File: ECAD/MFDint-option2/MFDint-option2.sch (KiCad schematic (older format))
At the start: 40 parts, among them J1 Conn_02x03_Odd_Even, J2 Conn_01x04, J3 Conn_01x04, J4 Conn_02x03_Odd_Even, J5 Conn_01x04, J6 Conn_01x04, SW11 SW_Push, SW12 SW_Push, SW13 SW_Push, SW14 SW_Push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

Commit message: Removing panelisations, adding polyfuses
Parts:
- added F1, F2: Polyfuse, Fuse:Fuse_1206_3216Metric_Pad1.42x1.75mm_HandSolder, symbol Device:Polyfuse
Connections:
- wire segments 176 -> 184
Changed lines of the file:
@@
 	1    0    0    -1
 $EndComp
-$Comp
-L power:+5V #PWR0104
-U 1 1 60C40200
-P 3650 750
-F 0 "#PWR0104" H 3650 600 50  0001 C CNN
-F 1 "+5V" H 3665 923 50  0000 C CNN
-F 2 "" H 3650 750 50  0001 C CNN
-F 3 "" H 3650 750 50  0001 C CNN
-	1    3650 750
-	1    0    0    -1
-$EndComp
-Wire Wire Line
-	3650 750  3700 750
 Wire Wire Line
 	3700 850  3650 850
@@
 L power:+5V #PWR0108
 U 1 1 60D08791
-P 3650 1500
-F 0 "#PWR0108" H 3650 1350 50  0001 C CNN
-F 1 "+5V" H 3665 1673 50  0000 C CNN
-F 2 "" H 3650 1500 50  0001 C CNN
-F 3 "" H 3650 1500 50  0001 C CNN
-	1    3650 1500
-	1    0    0    -1
-$EndComp
-Wire Wire Line
-	3650 1500 3700 1500
+P 4900 600
+F 0 "#PWR0108" H 4900 450 50  0001 C CNN
+F 1 "+5V" H 4915 773 50  0000 C CNN
+F 2 "" H 4900 600 50  0001 C CNN
+F 3 "" H 4900 600 50  0001 C CNN
+	1    4900 600
+	1    0    0    -1
+$EndComp
 Wire Wire Line
 	3700 1600 3650 1600
@@
 	1    0    0    -1
 $EndComp
-Wire Wire Line
-	9350 950  9400 950
 Wire Wire Line
 	9400 1050 9350 1050
@@
 	1    0    0    -1
 $EndComp
-Wire Wire Line
-	9350 1700 9400 1700
 Wire Wire Line
 	9400 1800 9350 1800
@@
 L power:VCC #PWR0113
 U 1 1 60DE50D9
-P 9350 950
-F 0 "#PWR0113" H 9350 800 50  0001 C CNN
-F 1 "VCC" H 9365 1123 50  0000 C CNN
-F 2 "" H 9350 950 50  0001 C CNN
-F 3 "" H 9350 950 50  0001 C CNN
-	1    9350 950
-	1    0    0    -1
-$EndComp
-$Comp
-L power:VCC #PWR0114
-U 1 1 60DEBA77
-P 9350 1700
-F 0 "#PWR0114" H 9350 1550 50  0001 C CNN
-F 1 "VCC" H 9365 1873 50  0000 C CNN
-F 2 "" H 9350 1700 50  0001 C CNN
-F 3 "" H 9350 1700 50  0001 C CNN
-	1    9350 1700
+P 10600 800
+F 0 "#PWR0113" H 10600 650 50  0001 C CNN
+F 1 "VCC" H 10615 973 50  0000 C CNN
+F 2 "" H 10600 800 50  0001 C CNN
+F 3 "" H 10600 800 50  0001 C CNN
+	1    10600 800
 	1    0    0    -1
 $EndComp
@@
 Wire Wire Line
 	9750 5250 10650 5250
+$Comp
+L Device:Polyfuse F1
+U 1 1 60F99DDE
+P 4600 600
+F 0 "F1" V 4375 600 50  0000 C CNN
+F 1 "Polyfuse" V 4466 600 50  0000 C CNN
+F 2 "Fuse:Fuse_1206_3216Metric_Pad1.42x1.75mm_HandSolder" H 4650 400 50  0001 L CNN
+F 3 "~" H 4600 600 50  0001 C CNN
+	1    4600 600
+	0    1    1    0
+$EndComp
+Wire Wire Line
+	3400 750  3400 1500
+Wire Wire Line
+	3400 750  3700 750
+Wire Wire Line
+	3400 1500 3700 1500
+Wire Wire Line
+	3400 750  3400 600
+Wire Wire Line
+	3400 600  4450 600
+Connection ~ 3400 750
+Wire Wire Line
+	4750 600  4900 600
+Wire Wire Line
+	9100 950  9100 1700
+Wire Wire Line
+	9100 950  9100 800
+Wire Wire Line
+	9100 800  10150 800
+Connection ~ 9100 950
+Wire Wire Line
+	9100 950  9400 950
+Wire Wire Line
+	9100 1700 9400 1700
+$Comp
+L Device:Polyfuse F2
+U 1 1 60FC34AB
+P 10300 800
+F 0 "F2" V 10075 800 50  0000 C CNN
+F 1 "Polyfuse" V 10166 800 50  0000 C CNN
+F 2 "Fuse:Fuse_1206_3216Metric_Pad1.42x1.75mm_HandSolder" H 10350 600 50  0001 L CNN
+F 3 "~" H 10300 800 50  0001 C CNN
+	1    10300 800
+	0    1    1    0
+$EndComp
+Wire Wire Line
+	10450 800  10600 800
 $EndSCHEMATC

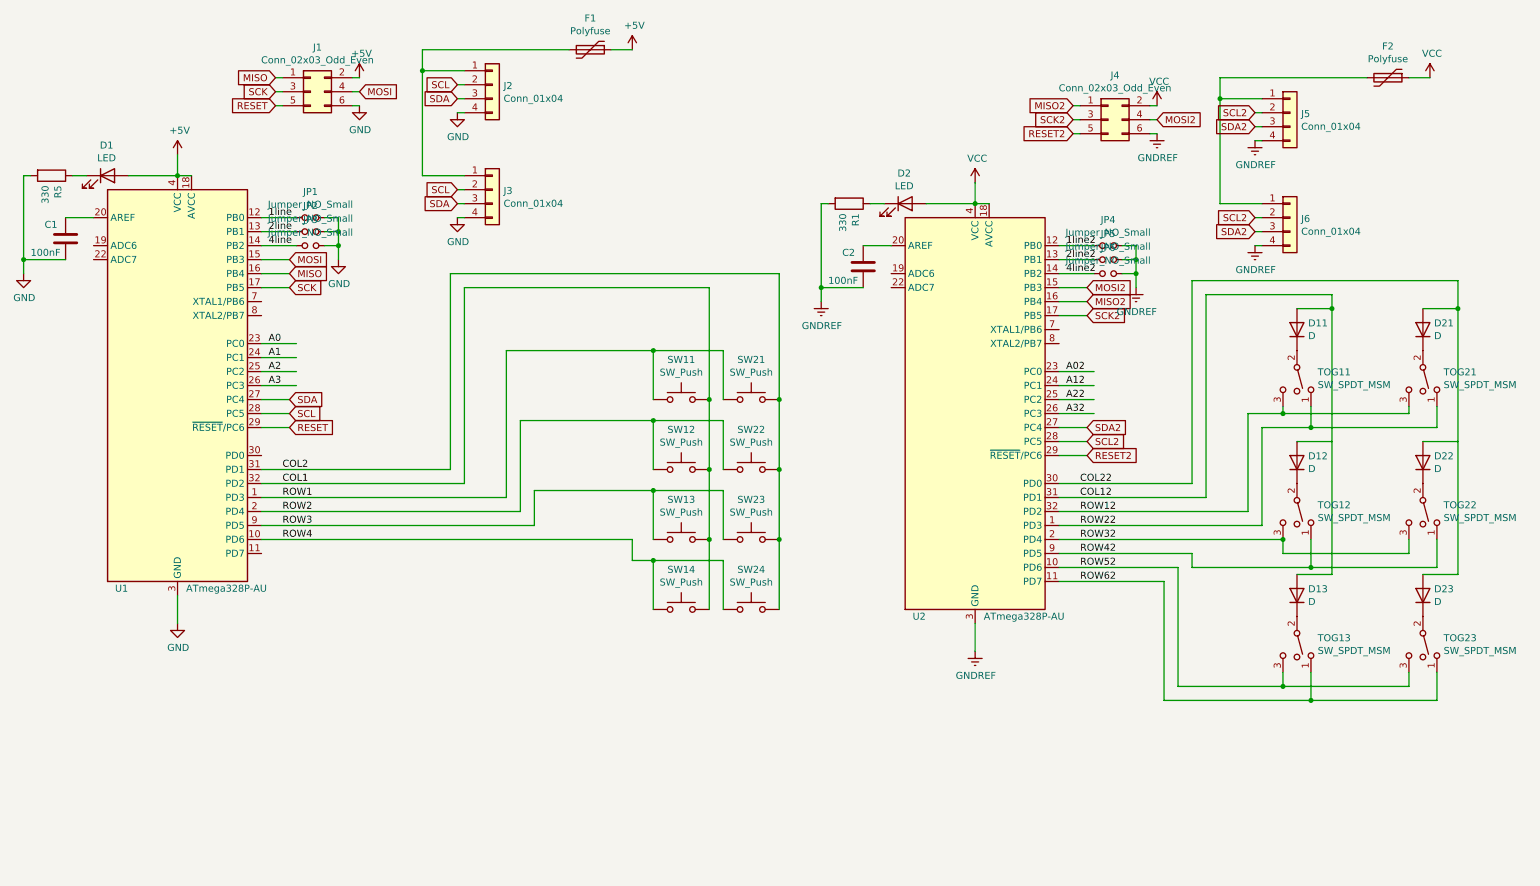
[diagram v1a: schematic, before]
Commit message: Change from 1x04 2.54mm headers to 1x05 micro JST
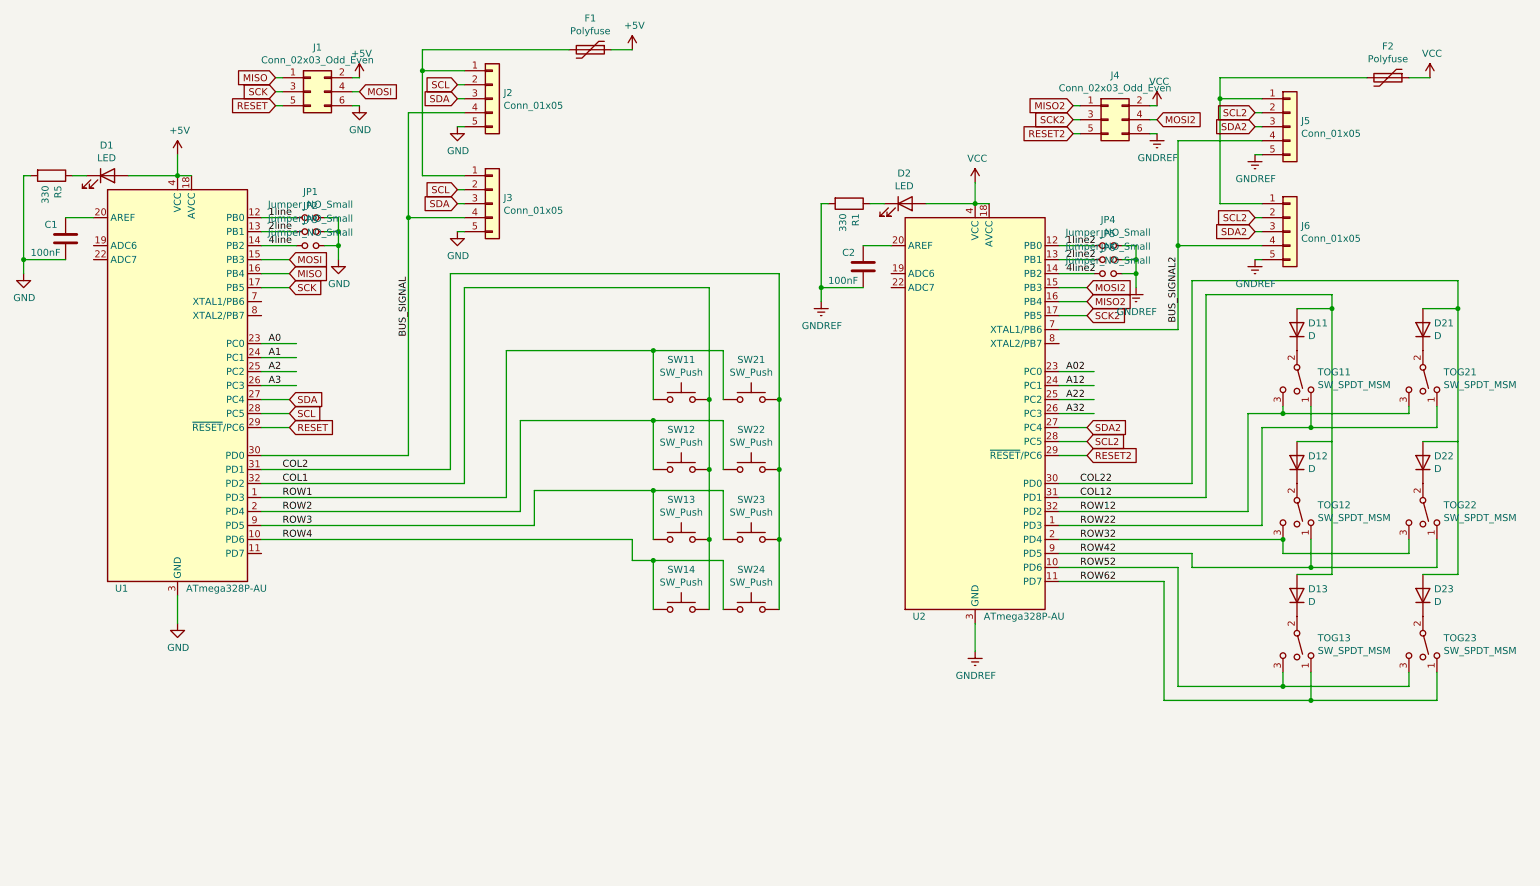
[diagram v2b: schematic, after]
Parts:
- removed J2, J3, J5, J6: Conn_01x04, mycustomlibrary:PinHeader_1x04_P2.54mm_Horizontal_SMD, symbol Connector_Generic:Conn_01x04
- added J2, J3, J5, J6: Conn_01x05, Connector_JST:JST_GH_SM05B-GHS-TB_1x05-1MP_P1.25mm_Horizontal, symbol Connector_Generic:Conn_01x05
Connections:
- net labels added: BUS_SIGNAL, BUS_SIGNAL2
- wire segments 184 -> 194
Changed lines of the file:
@@
 Wire Wire Line
 	2250 2300 2450 2300
-$Comp
-L Connector_Generic:Conn_01x04 J2
-U 1 1 60C3EB30
-P 3900 850
-F 0 "J2" H 3980 842 50  0000 L CNN
-F 1 "Conn_01x04" H 3980 751 50  0000 L CNN
-F 2 "mycustomlibrary:PinHeader_1x04_P2.54mm_Horizontal_SMD" H 3900 850 50  0001 C CNN
-F 3 "~" H 3900 850 50  0001 C CNN
-	1    3900 850
-	1    0    0    -1
-$EndComp
 Text GLabel 3650 850  0    50   Input ~ 0
 SCL
@@
 L power:GND #PWR0103
 U 1 1 60C3FBB7
-P 3650 1050
-F 0 "#PWR0103" H 3650 800 50  0001 C CNN
-F 1 "GND" H 3655 877 50  0000 C CNN
-F 2 "" H 3650 1050 50  0001 C CNN
-F 3 "" H 3650 1050 50  0001 C CNN
-	1    3650 1050
+P 3650 1150
+F 0 "#PWR0103" H 3650 900 50  0001 C CNN
+F 1 "GND" H 3655 977 50  0000 C CNN
+F 2 "" H 3650 1150 50  0001 C CNN
+F 3 "" H 3650 1150 50  0001 C CNN
+	1    3650 1150
 	1    0    0    -1
 $EndComp
@@
 	3650 950  3700 950
 Wire Wire Line
-	3700 1050 3650 1050
+	3700 1150 3650 1150
 $Comp
 L Connector_Generic:Conn_02x03_Odd_Even J1
@@
 	1    0    0    -1
 $EndComp
-$Comp
-L Connector_Generic:Conn_01x04 J3
-U 1 1 60D08783
-P 3900 1600
-F 0 "J3" H 3980 1592 50  0000 L CNN
-F 1 "Conn_01x04" H 3980 1501 50  0000 L CNN
-F 2 "mycustomlibrary:PinHeader_1x04_P2.54mm_Horizontal_SMD" H 3900 1600 50  0001 C CNN
-F 3 "~" H 3900 1600 50  0001 C CNN
-	1    3900 1600
-	1    0    0    -1
-$EndComp
 Text GLabel 3650 1600 0    50   Input ~ 0
 SCL
@@
 L power:GND #PWR0107
 U 1 1 60D0878B
-P 3650 1800
-F 0 "#PWR0107" H 3650 1550 50  0001 C CNN
-F 1 "GND" H 3655 1627 50  0000 C CNN
-F 2 "" H 3650 1800 50  0001 C CNN
-F 3 "" H 3650 1800 50  0001 C CNN
-	1    3650 1800
+P 3650 1900
+F 0 "#PWR0107" H 3650 1650 50  0001 C CNN
+F 1 "GND" H 3655 1727 50  0000 C CNN
+F 2 "" H 3650 1900 50  0001 C CNN
+F 3 "" H 3650 1900 50  0001 C CNN
+	1    3650 1900
 	1    0    0    -1
 $EndComp
@@
 	3650 1700 3700 1700
 Wire Wire Line
-	3700 1800 3650 1800
+	3700 1900 3650 1900
 Wire Wire Line
 	2500 2000 2250 2000
@@
 Wire Wire Line
 	7950 2500 8150 2500
-$Comp
-L Connector_Generic:Conn_01x04 J5
-U 1 1 60DC1519
-P 9600 1050
-F 0 "J5" H 9680 1042 50  0000 L CNN
-F 1 "Conn_01x04" H 9680 951 50  0000 L CNN
-F 2 "mycustomlibrary:PinHeader_1x04_P2.54mm_Horizontal_SMD" H 9600 1050 50  0001 C CNN
-F 3 "~" H 9600 1050 50  0001 C CNN
-	1    9600 1050
-	1    0    0    -1
-$EndComp
 Wire Wire Line
 	9400 1050 9350 1050
@@
 	9350 1150 9400 1150
 Wire Wire Line
-	9400 1250 9350 1250
+	9400 1350 9350 1350
 $Comp
 L Connector_Generic:Conn_02x03_Odd_Even J4
@@
 Wire Wire Line
 	7000 1700 7350 1700
-$Comp
-L Connector_Generic:Conn_01x04 J6
-U 1 1 60DC15D0
-P 9600 1800
-F 0 "J6" H 9680 1792 50  0000 L CNN
-F 1 "Conn_01x04" H 9680 1701 50  0000 L CNN
-F 2 "mycustomlibrary:PinHeader_1x04_P2.54mm_Horizontal_SMD" H 9600 1800 50  0001 C CNN
-F 3 "~" H 9600 1800 50  0001 C CNN
-	1    9600 1800
-	1    0    0    -1
-$EndComp
 Wire Wire Line
 	9400 1800 9350 1800
@@
 	9350 1900 9400 1900
 Wire Wire Line
-	9400 2000 9350 2000
+	9400 2100 9350 2100
 Wire Wire Line
 	8200 2200 7950 2200
@@
 L power:GNDREF #PWR0115
 U 1 1 60DF276B
-P 9350 2000
-F 0 "#PWR0115" H 9350 1750 50  0001 C CNN
-F 1 "GNDREF" H 9355 1827 50  0000 C CNN
-F 2 "" H 9350 2000 50  0001 C CNN
-F 3 "" H 9350 2000 50  0001 C CNN
-	1    9350 2000
+P 9350 2100
+F 0 "#PWR0115" H 9350 1850 50  0001 C CNN
+F 1 "GNDREF" H 9355 1927 50  0000 C CNN
+F 2 "" H 9350 2100 50  0001 C CNN
+F 3 "" H 9350 2100 50  0001 C CNN
+	1    9350 2100
 	1    0    0    -1
 $EndComp
@@
 L power:GNDREF #PWR0116
 U 1 1 60DF3B71
-P 9350 1250
-F 0 "#PWR0116" H 9350 1000 50  0001 C CNN
-F 1 "GNDREF" H 9355 1077 50  0000 C CNN
-F 2 "" H 9350 1250 50  0001 C CNN
-F 3 "" H 9350 1250 50  0001 C CNN
-	1    9350 1250
+P 9350 1350
+F 0 "#PWR0116" H 9350 1100 50  0001 C CNN
+F 1 "GNDREF" H 9355 1177 50  0000 C CNN
+F 2 "" H 9350 1350 50  0001 C CNN
+F 3 "" H 9350 1350 50  0001 C CNN
+	1    9350 1350
 	1    0    0    -1
 $EndComp
@@
 Wire Wire Line
 	10450 800  10600 800
+$Comp
+L Connector_Generic:Conn_01x05 J5
+U 1 1 611EB8F1
+P 9600 1150
+F 0 "J5" H 9680 1192 50  0000 L CNN
+F 1 "Conn_01x05" H 9680 1101 50  0000 L CNN
+F 2 "Connector_JST:JST_GH_SM05B-GHS-TB_1x05-1MP_P1.25mm_Horizontal" H 9600 1150 50  0001 C CNN
+F 3 "~" H 9600 1150 50  0001 C CNN
+	1    9600 1150
+	1    0    0    -1
+$EndComp
+$Comp
+L Connector_Generic:Conn_01x05 J6
+U 1 1 611ED7B6
+P 9600 1900
+F 0 "J6" H 9680 1942 50  0000 L CNN
+F 1 "Conn_01x05" H 9680 1851 50  0000 L CNN
+F 2 "Connector_JST:JST_GH_SM05B-GHS-TB_1x05-1MP_P1.25mm_Horizontal" H 9600 1900 50  0001 C CNN
+F 3 "~" H 9600 1900 50  0001 C CNN
+	1    9600 1900
+	1    0    0    -1
+$EndComp
+$Comp
+L Connector_Generic:Conn_01x05 J2
+U 1 1 611F6121
+P 3900 950
+F 0 "J2" H 3980 992 50  0000 L CNN
+F 1 "Conn_01x05" H 3980 901 50  0000 L CNN
+F 2 "Connector_JST:JST_GH_SM05B-GHS-TB_1x05-1MP_P1.25mm_Horizontal" H 3900 950 50  0001 C CNN
+F 3 "~" H 3900 950 50  0001 C CNN
+	1    3900 950
+	1    0    0    -1
+$EndComp
+$Comp
+L Connector_Generic:Conn_01x05 J3
+U 1 1 611FE98A
+P 3900 1700
+F 0 "J3" H 3980 1742 50  0000 L CNN
+F 1 "Conn_01x05" H 3980 1651 50  0000 L CNN
+F 2 "Connector_JST:JST_GH_SM05B-GHS-TB_1x05-1MP_P1.25mm_Horizontal" H 3900 1700 50  0001 C CNN
+F 3 "~" H 3900 1700 50  0001 C CNN
+	1    3900 1700
+	1    0    0    -1
+$EndComp
+Wire Wire Line
+	2250 3500 3300 3500
+Wire Wire Line
+	3300 3500 3300 1800
+Wire Wire Line
+	3300 1050 3700 1050
+Wire Wire Line
+	3700 1800 3300 1800
+Connection ~ 3300 1800
+Wire Wire Line
+	3300 1800 3300 1050
+Wire Wire Line
+	7950 2600 8800 2600
+Wire Wire Line
+	8800 2600 8800 2000
+Wire Wire Line
+	8800 2000 9400 2000
+Wire Wire Line
+	9400 1250 8800 1250
+Wire Wire Line
+	8800 1250 8800 2000
+Connection ~ 8800 2000
+Text Label 3300 2650 1    50   ~ 0
+BUS_SIGNAL
+Text Label 8800 2550 1    50   ~ 0
+BUS_SIGNAL2
 $EndSCHEMATC

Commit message: Swap bus connector to 4-pin JST-GH
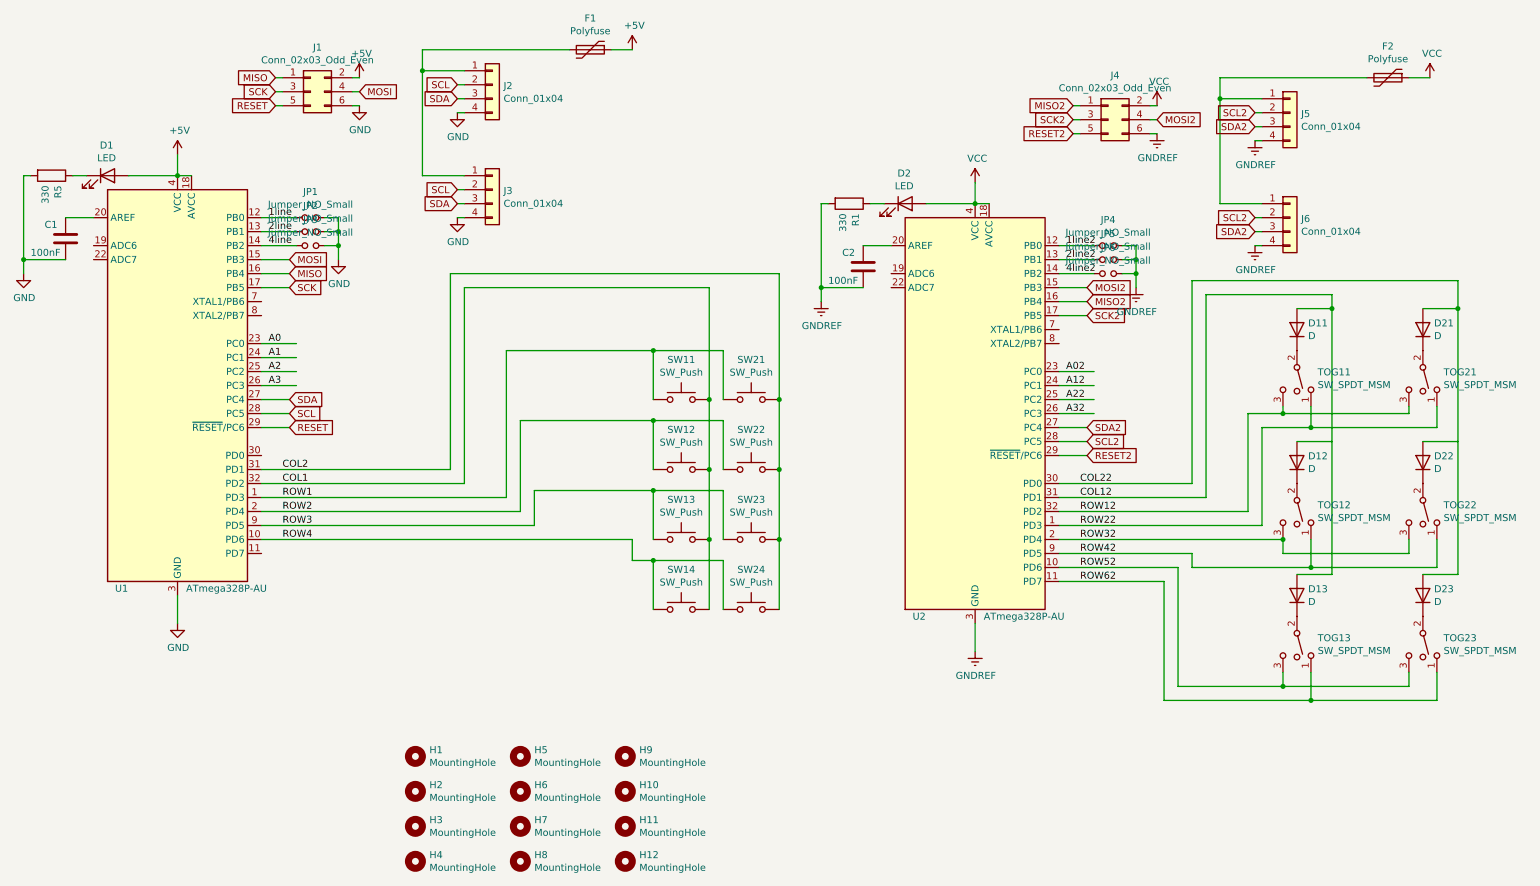
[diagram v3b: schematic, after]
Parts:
- removed J2, J3, J5, J6: Conn_01x05, Connector_JST:JST_GH_SM05B-GHS-TB_1x05-1MP_P1.25mm_Horizontal, symbol Connector_Generic:Conn_01x05
- added H1, H2, H3, H4: MountingHole, MountingHole:MountingHole_4.3mm_M4, symbol Mechanical:MountingHole
- added H10, H11, H12, H5, H6, H7, H8, H9: MountingHole, MountingHole:MountingHole_3.2mm_M3, symbol Mechanical:MountingHole
- added J2, J3, J5, J6: Conn_01x04, Connector_JST:JST_GH_SM04B-GHS-TB_1x04-1MP_P1.25mm_Horizontal, symbol Connector_Generic:Conn_01x04
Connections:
- net labels removed: BUS_SIGNAL, BUS_SIGNAL2
- wire segments 194 -> 184
